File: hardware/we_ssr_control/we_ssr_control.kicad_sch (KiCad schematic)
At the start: 25 parts, among them Q1 IRF4905, U1 WeMos_D1_mini, U2 ULN2803A

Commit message: WIP control connector changes
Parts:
- removed REG1: LM7805, Package_TO_SOT_SMD:SOT-223, symbol SamacSys_Parts:LM7805MPX_NOPB
- added H4: MountingHole_Pad, MountingHole:MountingHole_3.2mm_M3_Pad_Via, symbol Mechanical:MountingHole_Pad
- added JL1: Conn_01x02, Connector_PinHeader_1.00mm:PinHeader_1x02_P1.00mm_Vertical, symbol Connector_Generic:Conn_01x02
- added REG1: LM7805, Package_TO_SOT_SMD:SOT-223, symbol We_control:LM7805MPX_NOPB
- Q1: Height 4.69 -> (none); Height (mm) (none) -> 4.69; MFN (none) -> Infineon; MFP (none) -> IRF4905PBF; Manufacturer_Name Infineon -> (none); Manufacturer_Part_Number IRF4905PBF -> (none); Mouser Part Number 942-IRF4905PBF -> (none); Package (none) -> TO-254; Type (none) -> THT
- S1: footprint Picow_control:1938MS -> We_control:1938MS; symbol Picow_control:193-8MS -> We_control:193-8MS
- U1: symbol MCU_Module:WeMos_D1_mini -> We_control:WeMos_D1_mini; MFN (none) -> WEMOS; MFP (none) -> D1 Mini; Package (none) -> Other; Type (none) -> Other; now left out of the parts list
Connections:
- net +5V: now also REG1.3 (OUTPUT)
- net +VDC: now also REG1.1 (INPUT)
- net GNDPWR: now also H4.1, JL1.1 (Pin_1), REG1.2 (GND_1), REG1.4 (GND_2)
- net at LED1.2, RL1.2: now also JL1.2 (Pin_2)
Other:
- note added: "Power Management / Regulation"
- note added: "Primary Control"
- note removed: "Automatic Control"
- note removed: "Power Control / Regulation"
- moved on the sheet: C2, JP1, LED1, RL1

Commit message: WIP for updated layout
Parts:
- removed C3: 100n, Capacitor_SMD:C_0805_2012Metric, symbol Device:C
- removed H4: MountingHole_Pad, MountingHole:MountingHole_3.2mm_M3_Pad_Via, symbol Mechanical:MountingHole_Pad
- removed JCNTL1: Conn_02x06_Odd_Even, Connector_IDC:IDC-Header_2x06_P2.54mm_Horizontal, symbol Connector_Generic:Conn_02x06_Odd_Even
- removed U2: ULN2803A, Package_DIP:DIP-18_W7.62mm, symbol Transistor_Array:ULN2805A
- added FID1, FID2, FID3: Fiducial, Fiducial:Fiducial_0.5mm_Mask1mm, symbol Mechanical:Fiducial
- added JCNTL1, JCNTL2: SHF-105-01-L-D-RA, dragon_mobile:SAMTEC_SHF-105-01-L-D-RA, symbol Connector_Samtec:SHF-105-01-L-D-RA
- added JS1: SolderJumper_3_Bridged12, Jumper:SolderJumper-3_P1.3mm_Bridged12_RoundedPad1.0x1.5mm_NumberLabels, symbol Jumper:SolderJumper_3_Bridged12
- added JS2: Conn_01x02, Connector_PinHeader_1.00mm:PinHeader_1x02_P1.00mm_Vertical, symbol Connector_Generic:Conn_01x02
- added QD1, QD2, QD3, QD4, QD5, QD6, QD7, QD8: 2N7002K, Package_TO_SOT_SMD:SOT-23, symbol Transistor_FET:2N7002K
- JL1: now in the parts list
- RS1, RS2, RS3, RS4, RS5, RS6, RS7, RS8: value 25 -> 270; Characteristics (none) -> 270Ohms; 300mW; SMD (0603) 5% Anti Surge AEC-Q200; MFN (none) -> ROHM Semiconductor; MFP (none) -> SDR03EZPJ271; Mouser Part Number (none) -> 755-SDR03EZPJ271; Mouser Price/Stock (none) -> https://www.mouser.com/ProductDetail/ROHM-Semiconductor/SDR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; Package (none) -> 0603; Type (none) -> SMD
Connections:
- net +BATT: now also JS1.2 (C), JS2.1 (Pin_1)
- net GNDPWR: now also JCNTL1.10, JCNTL1.2, JCNTL1.4, JCNTL1.6, JCNTL1.8, JCNTL2.10, JCNTL2.2, JCNTL2.4, JCNTL2.6, JCNTL2.8, JS2.2 (Pin_2), QD1.2 (S), QD2.2 (S), QD3.2 (S), QD4.2 (S), QD5.2 (S), QD6.2 (S), QD7.2 (S), QD8.2 (S)
- net a1: now also RS1.1, QD1.3 (D); no longer RS1.2
- net a2: now also QD2.3 (D)
- net a3: now also RS3.1, QD3.3 (D); no longer RS3.2
- net a4: now also QD4.3 (D)
- net a5: now also S1.16, QD5.3 (D); no longer S1.13
- net a6: now also RS6.1, S1.15, QD6.3 (D); no longer RS6.2, S1.14
- net a7: now also S1.14, QD7.3 (D); no longer S1.15
- net a8: now also RS8.1, S1.13, QD8.3 (D); no longer RS8.2, S1.16
- net b1: now reaches U1.11 (D4)
- net b1: now also QD1.1 (G)
- net b2: now reaches U1.12 (D3)
- net b2: now also QD2.1 (G)
- net b3: now reaches U1.13 (SDA/D2)
- net b3: now also QD3.1 (G)
- net b4: now reaches U1.14 (SCL/D1)
- net b4: now also QD4.1 (G)
- net b8: now reaches U1.4 (SCK/D5)
- net b8: now also QD8.1 (G)
- net b7: now reaches U1.5 (MISO/D6)
- net b7: now also QD7.1 (G)
- net b6: now reaches U1.6 (MOSI/D7)
- net b6: now also QD6.1 (G)
- net b5: now reaches U1.7 (CS/D8)
- net b5: now also QD5.1 (G)
- net at RS2.2: now also JCNTL1.5
- net at RS4.2: now also JCNTL1.9
- net at RS5.2: now also JCNTL2.7
- net at RS7.2: now also JCNTL2.3
- new net: JCNTL2.1, RS8.2
- new net: JCNTL1.3, RS1.2
- new net: JCNTL1.1, JS1.1 (A)
- new net: JCNTL2.9, JS1.3 (B)
- new net: JCNTL2.5, RS6.2
- new net: JCNTL1.7, RS3.2
- no-connect marks 1 -> 6
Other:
- note added: "Control outputs are active LOW / open drain (collector) By default the input voltage is taken from Pin 1 on JCNTL1 but maybe switched to Pin 9 on JCNTL2 or both if connect to a single SSR board. Optional both can be disconnected and power supplied via JS2 but care must be taken to insure there is a common ground between this control board, power input, and the SSR board."
- note added: "Fiducials"
- note added: "WeMOS Control / Drivers"
- note removed: "Outputs are active LOW / open collector"
- note removed: "Primary Control"
- moved on the sheet: C1, C2, H1, H2, H3, JL1, JP1, LED1, REG1, RL1, RP1, S1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

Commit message: Minor updates for v0.0.9
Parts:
- JCNTL1, JCNTL2: Height (mm) (none) -> 5.33; MANUFACTURER Samtec -> (none); MFN (none) -> Samtec; MFP (none) -> SHF-105-01-L-D-RA-TR; Mouser Part Number (none) -> 200-SHF10501LDRATR; Mouser Price/Stock (none) -> https://www.mouser.com/ProductDetail/Samtec/SHF-105-01-L-D-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; PARTREV R -> (none); Package (none) -> Other; STANDARD Manufacturer Recommendations -> (none)
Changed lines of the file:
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@@
   (title_block
     (title "Dragon We SSR Control")
-    (date "2023-01-03")
-    (rev "0.0.8")
+    (date "2023-01-10")
+    (rev "0.0.9")
     (comment 2 "creativecommons.org/licenses/by/4.0/")
     (comment 3 "License: CC By 4.0")
@@
   (junction (at 189.23 45.72) (diameter 0) (color 0 0 0 0)
   )
+  (junction (at 124.46 88.9) (diameter 0) (color 0 0 0 0)
+  )
   (junction (at 71.12 71.12) (diameter 0) (color 0 0 0 0)
-  )
-  (junction (at 124.46 101.6) (diameter 0) (color 0 0 0 0)
   )
   (junction (at 187.96 154.94) (diameter 0) (color 0 0 0 0)
@@
     (stroke (width 0) (type default) (color 0 0 0 0))
   )
+  (bus (pts (xy 124.46 88.9) (xy 124.46 91.44))
+    (stroke (width 0) (type default) (color 0 0 0 0))
+  )
   (wire (pts (xy 240.03 40.64) (xy 242.57 40.64))
     (stroke (width 0) (type default) (color 0 0 0 0))
@@
     (stroke (width 0) (type default) (color 0 0 0 0))
   )
+  (bus (pts (xy 124.46 88.9) (xy 109.22 88.9))
+    (stroke (width 0) (type default) (color 0 0 0 0))
+  )
   (bus (pts (xy 187.96 127) (xy 190.5 127))
     (stroke (width 0) (type default) (color 0 0 0 0))
@@
     (stroke (width 0) (type default) (color 0 0 0 0))
   )
-  (bus (pts (xy 124.46 91.44) (xy 124.46 101.6))
+  (bus (pts (xy 124.46 91.44) (xy 124.46 106.68))
     (stroke (width 0) (type default) (color 0 0 0 0))
   )
@@
     (stroke (width 0) (type default) (color 0 0 0 0))
   )
-  (bus (pts (xy 109.22 101.6) (xy 124.46 101.6))
-    (stroke (width 0) (type default) (color 0 0 0 0))
-  )
   (polyline (pts (xy 15.24 83.82) (xy 15.24 121.92))
     (stroke (width 0) (type default) (color 0 0 0 0))
@@
     (stroke (width 0) (type default) (color 0 0 0 0))
   )
-  (bus (pts (xy 124.46 81.28) (xy 124.46 91.44))
+  (bus (pts (xy 124.46 81.28) (xy 124.46 88.9))
     (stroke (width 0) (type default) (color 0 0 0 0))
   )
@@
     (stroke (width 0) (type default) (color 0 0 0 0))
   )
-  (bus (pts (xy 109.22 101.6) (xy 109.22 114.3))
+  (bus (pts (xy 109.22 88.9) (xy 109.22 114.3))
     (stroke (width 0) (type default) (color 0 0 0 0))
   )
@@
   )
   (polyline (pts (xy 15.24 127) (xy 38.1 127))
-    (stroke (width 0) (type default) (color 0 0 0 0))
-  )
-  (bus (pts (xy 124.46 101.6) (xy 124.46 106.68))
     (stroke (width 0) (type default) (color 0 0 0 0))
   )
@@
       (effects (font (size 1.27 1.27)) (justify bottom) hide)
     )
-    (property "Datasheet" "~" (id 3) (at 249.555 45.72 0)
-      (effects (font (size 1.27 1.27)) hide)
-    )
-    (property "PARTREV" "R" (id 4) (at 238.76 69.85 0)
-      (effects (font (size 1.27 1.27)) (justify bottom) hide)
-    )
-    (property "STANDARD" "Manufacturer Recommendations" (id 5) (at 252.73 66.04 0)
-      (effects (font (size 1.27 1.27)) (justify bottom) hide)
-    )
-    (property "MANUFACTURER" "Samtec" (id 6) (at 241.3 67.945 0)
-      (effects (font (size 1.27 1.27)) (justify bottom) hide)
+    (property "Datasheet" "https://www.mouser.com/datasheet/2/527/shf-2854584.pdf" (id 3) (at 249.555 45.72 0)
+      (effects (font (size 1.27 1.27)) hide)
+    )
+    (property "Description" "Headers & Wire Housings Shrouded Terminal Strip, 0.050\"(1.27mm) pitch, Pin(Male), Right Angle, IDC; 10 Pos. 2 Rows;" (id 7) (at 297.18 76.2 0)
+      (effects (font (size 1.27 1.27)) hide)
+    )
+    (property "Height (mm)" "5.33" (id 8) (at 240.665 73.66 0)
+      (effects (font (size 1.27 1.27)) hide)
+    )
+    (property "MFN" "Samtec" (id 9) (at 249.555 45.72 0)
+      (effects (font (size 1.27 1.27)) hide)
+    )
+    (property "MFP" "SHF-105-01-L-D-RA-TR" (id 10) (at 249.555 45.72 0)
+      (effects (font (size 1.27 1.27)) hide)
+    )
+    (property "Package" "Other" (id 11) (at 249.555 45.72 0)
+      (effects (font (size 1.27 1.27)) hide)
+    )
+    (property "Mouser Part Number" "200-SHF10501LDRATR" (id 12) (at 249.555 45.72 0)
+      (effects (font (size 1.27 1.27)) hide)
+    )
+    (property "Mouser Price/Stock" "https://www.mouser.com/ProductDetail/Samtec/SHF-105-01-L-D-RA-TR?qs=%252BZP6%2F%252BtExtA3jdVUpsGHlg%3D%3D" (id 13) (at 249.555 45.72 0)
+      (effects (font (size 1.27 1.27)) hide)
     )
     (pin "1")
@@
     (pin "4")
   )
-  (symbol (lib_name "SHF-105-01-L-D-RA_1") (lib_id "Connector_Samtec:SHF-105-01-L-D-RA") (at 196.215 43.18 0) (mirror y) (unit 1)
+  (symbol (lib_id "Connector_Samtec:SHF-105-01-L-D-RA") (at 196.215 43.18 0) (mirror y) (unit 1)
     (in_bom yes) (on_board yes)
     (property "Reference" "JCNTL1" (id 0) (at 195.961 34.29 0))
@@
       (effects (font (size 1.27 1.27)) (justify bottom) hide)
     )
-    (property "Datasheet" "~" (id 3) (at 196.215 43.18 0)
-      (effects (font (size 1.27 1.27)) hide)
-    )
-    (property "PARTREV" "R" (id 4) (at 207.01 67.31 0)
-      (effects (font (size 1.27 1.27)) (justify bottom) hide)
-    )
-    (property "STANDARD" "Manufacturer Recommendations" (id 5) (at 193.04 63.5 0)
-      (effects (font (size 1.27 1.27)) (justify bottom) hide)
-    )
-    (property "MANUFACTURER" "Samtec" (id 6) (at 204.47 65.405 0)
-      (effects (font (size 1.27 1.27)) (justify bottom) hide)
-    )
-    (pin "1")
+    (property "Datasheet" "https://www.mouser.com/datasheet/2/527/shf-2854584.pdf" (id 3) (at 196.215 43.18 0)
+      (effects (font (size 1.27 1.27)) hide)
+    )
+    (property "Description" "Headers & Wire Housings Shrouded Terminal Strip, 0.050\"(1.27mm) pitch, Pin(Male), Right Angle, IDC; 10 Pos. 2 Rows;" (id 7) (at 148.59 73.66 0)
+      (effects (font (size 1.27 1.27)) hide)
+    )
+    (property "Height (mm)" "5.33" (id 8) (at 205.105 71.12 0)
+      (effects (font (size 1.27 1.27)) hide)
+    )
+    (property "MFN" "Samtec" (id 9) (at 196.215 43.18 0)
+      (effects (font (size 1.27 1.27)) hide)
+    )
+    (property "MFP" "SHF-105-01-L-D-RA-TR" (id 10) (at 196.215 43.18 0)
+      (effects (font (size 1.27 1.27)) hide)
+    )
+    (property "Package" "Other" (id 11) (at 196.215 43.18 0)
+      (effects (font (size 1.27 1.27)) hide)
+    )
+    (property "Mouser Part Number" "200-SHF10501LDRATR" (id 12) (at 196.215 43.18 0)
+      (effects (font (size 1.27 1.27)) hide)
+    )
+    (property "Mouser Price/Stock" "https://www.mouser.com/ProductDetail/Samtec/SHF-105-01-L-D-RA-TR?qs=%252BZP6%2F%252BtExtA3jdVUpsGHlg%3D%3D" (id 13) (at 196.215 43.18 0)
+      (effects (font (size 1.27 1.27)) hide)
+    )
+    (pin "1")

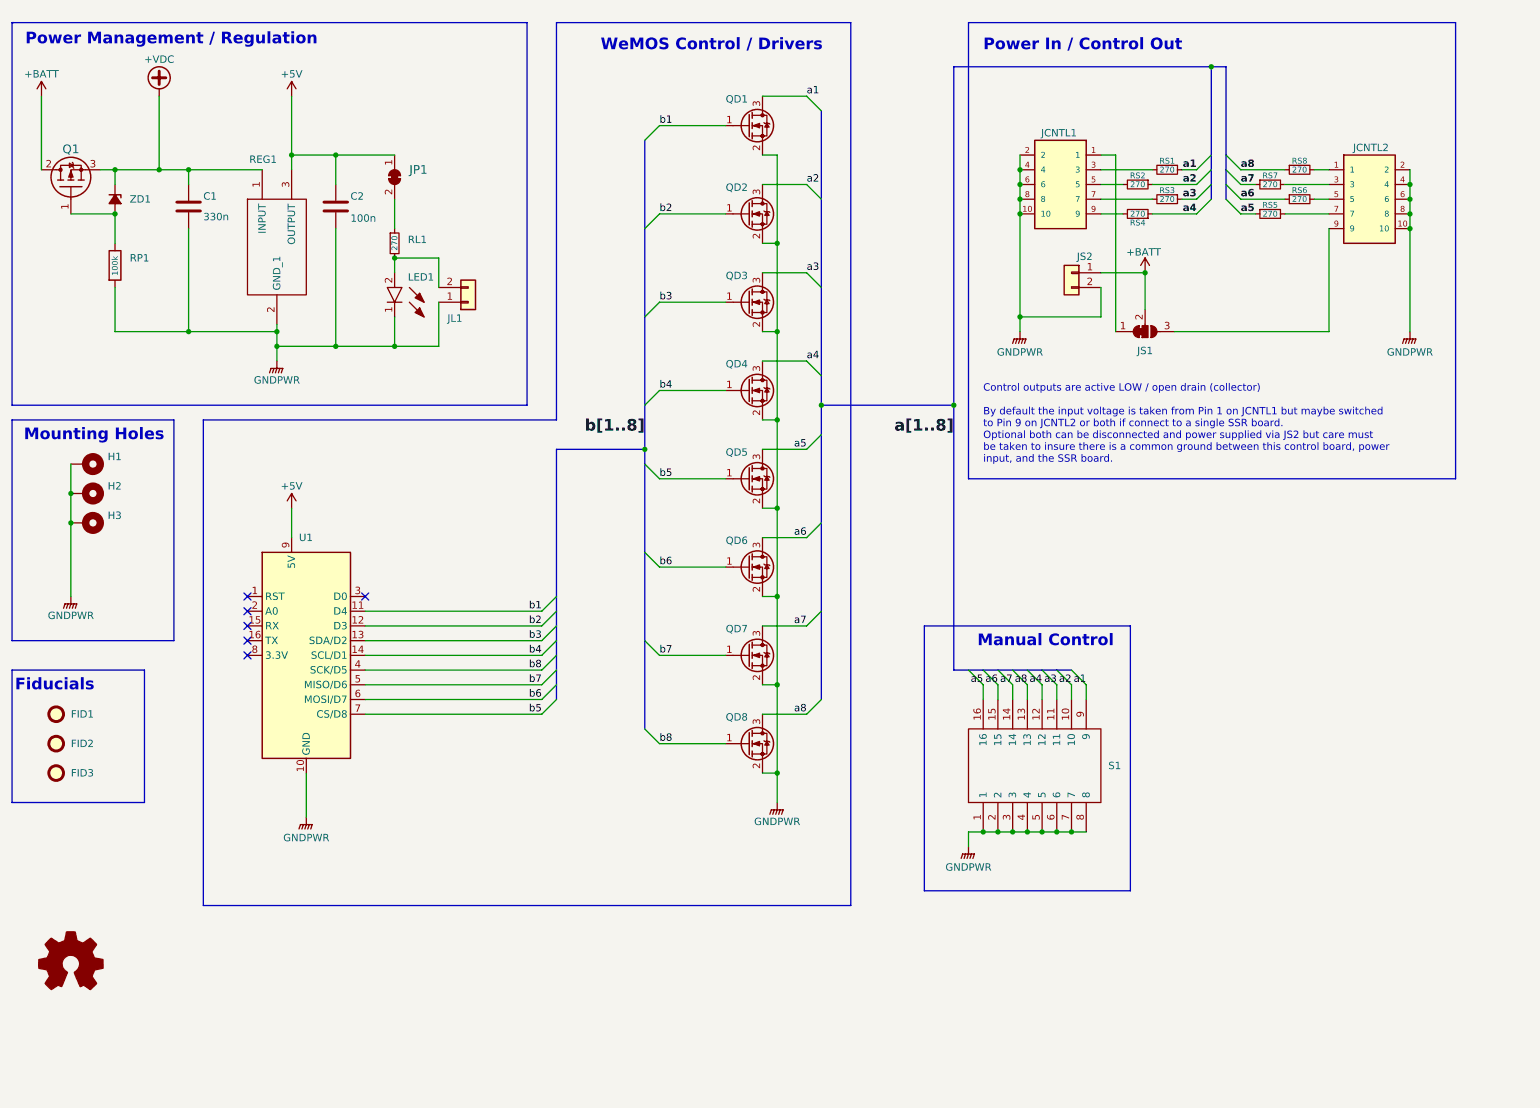
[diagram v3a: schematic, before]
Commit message: Changed schematic to hierarchical style with mutliple sheets
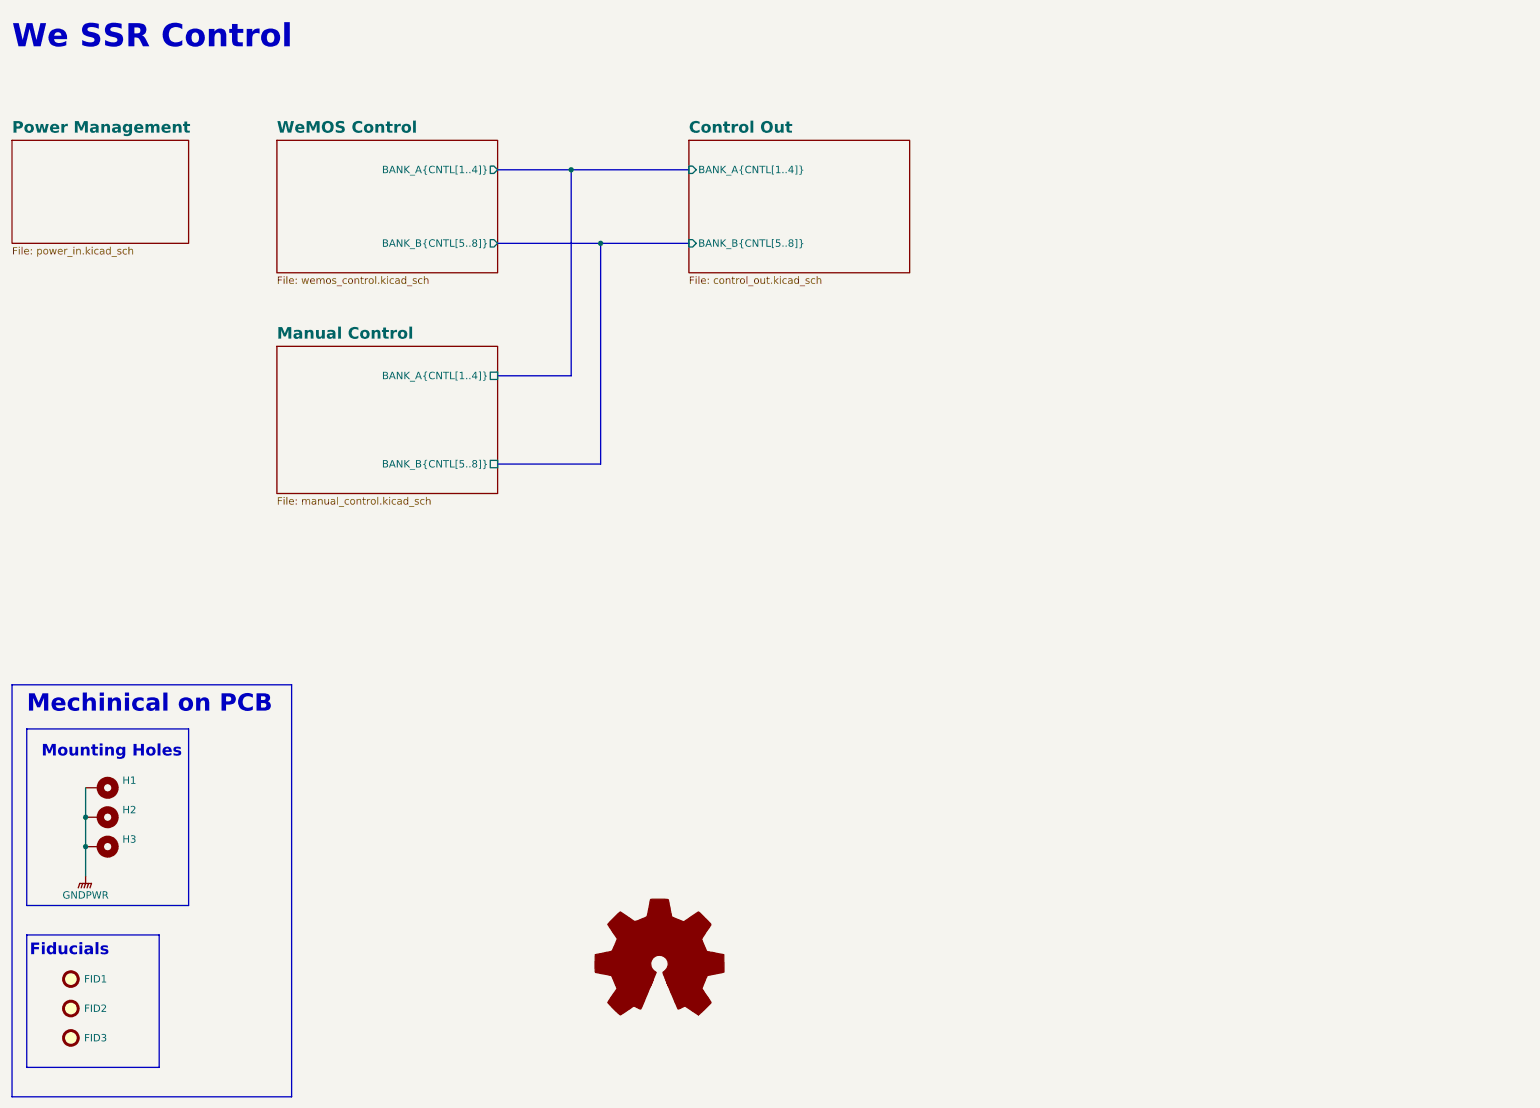
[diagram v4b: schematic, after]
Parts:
- removed C1: 330n, Capacitor_SMD:C_0805_2012Metric, symbol Device:C
- removed C2: 100n, Capacitor_SMD:C_0805_2012Metric, symbol Device:C
- removed JCNTL1, JCNTL2: SHF-105-01-L-D-RA, dragon_mobile:SAMTEC_SHF-105-01-L-D-RA, symbol Connector_Samtec:SHF-105-01-L-D-RA
- removed JL1, JS2: Conn_01x02, Connector_PinHeader_1.00mm:PinHeader_1x02_P1.00mm_Vertical, symbol Connector_Generic:Conn_01x02
- removed JP1: SolderJumper_2_Bridged, Jumper:SolderJumper-2_P1.3mm_Bridged_RoundedPad1.0x1.5mm, symbol Jumper:SolderJumper_2_Bridged
- removed JS1: SolderJumper_3_Bridged12, Jumper:SolderJumper-3_P1.3mm_Bridged12_RoundedPad1.0x1.5mm_NumberLabels, symbol Jumper:SolderJumper_3_Bridged12
- removed LED1: LTST-C190KGKT, dragon_mobile:LEDC1608X80N, symbol dragon_mobile:LTST-C190KGKT
- removed Q1: IRF4905, dragon_mobile:TO254P469X1042X1967-3P, symbol dragon_mobile:IRF4905PBF
- removed QD1, QD2, QD3, QD4, QD5, QD6, QD7, QD8: 2N7002K, Package_TO_SOT_SMD:SOT-23, symbol Transistor_FET:2N7002K
- removed REG1: LM7805, Package_TO_SOT_SMD:SOT-223, symbol We_control:LM7805MPX_NOPB
- removed RL1, RS1, RS2, RS3, RS4, RS5, RS6, RS7, RS8: 270, Resistor_SMD:R_0603_1608Metric, symbol Device:R_Small
- removed RP1: 100k, Resistor_SMD:R_0805_2012Metric, symbol Device:R
- removed S1: 193-8MS, We_control:1938MS, symbol We_control:193-8MS
- removed U1: WeMos_D1_mini, Module:WEMOS_D1_mini_light, symbol We_control:WeMos_D1_mini
- removed ZD1: +10v Zener Diode, Diode_SMD:D_SMF, symbol Device:D_Zener_Small_Filled
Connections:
- no-connect marks 6 -> 0
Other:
- added sheet Control Out (control_out.kicad_sch)
- added sheet Manual Control (manual_control.kicad_sch)
- added sheet Power Management (power_in.kicad_sch)
- added sheet WeMOS Control (wemos_control.kicad_sch)
- note added: "Mechinical on PCB"
- note added: "We SSR Control"
- note removed: "Control outputs are active LOW / open drain (collector) By default the input voltage is taken from Pin 1 on JCNTL1 but maybe switched to Pin 9 on JCNTL2 or both if connect to a single SSR board. Optional both can be disconnected and power supplied via JS2 but care must be taken to insure there is a common ground between this control board, power input, and the SSR board."
- note removed: "Manual Control"
- note removed: "Power In / Control Out"
- note removed: "Power Management / Regulation"
- note removed: "WeMOS Control / Drivers"
- title: Dragon We SSR Control -> We SSR Control
